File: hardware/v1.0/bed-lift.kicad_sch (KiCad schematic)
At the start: 64 parts, among them J1 SM04B-SRSS-TB, J2 S2P-VH, J3 SM04B-SRSS-TB, J4 S3B-XH-A, J5 S6B-XH-A, J6 Conn_ST_STDC14, J7 S6B-XH-A, J8 Conn_02x08_Odd_Even, Q1 MMBT3904, U1 LP2985-33DBVR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

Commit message: Review BOM.
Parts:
- C1, C11, C12, C13, C14, C15, C16, C2, C5, C8: Rating 50V, X5R -> 50V, X7R
- J8: now not fitted; now left out of the parts list
- U2: LCSC (none) -> C74511
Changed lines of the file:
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@@
 	(wire
 		(pts
-			(xy 118.11 214.63) (xy 124.46 214.63)
+			(xy 118.11 214.63) (xy 123.19 214.63)
 		)
 		(stroke
@@
 	(wire
 		(pts
-			(xy 120.65 203.2) (xy 124.46 203.2)
+			(xy 120.65 203.2) (xy 123.19 203.2)
 		)
 		(stroke
@@
 	(wire
 		(pts
-			(xy 119.38 200.66) (xy 124.46 200.66)
+			(xy 119.38 200.66) (xy 123.19 200.66)
 		)
 		(stroke
@@
 	(wire
 		(pts
-			(xy 118.11 209.55) (xy 124.46 209.55)
+			(xy 118.11 209.55) (xy 123.19 209.55)
 		)
 		(stroke
@@
 	(wire
 		(pts
-			(xy 121.92 205.74) (xy 124.46 205.74)
+			(xy 121.92 205.74) (xy 123.19 205.74)
 		)
 		(stroke
@@
 	(wire
 		(pts
-			(xy 118.11 217.17) (xy 124.46 217.17)
+			(xy 118.11 217.17) (xy 123.19 217.17)
 		)
 		(stroke
@@
 	(wire
 		(pts
-			(xy 118.11 219.71) (xy 124.46 219.71)
+			(xy 118.11 219.71) (xy 123.19 219.71)
 		)
 		(stroke
@@
 	(wire
 		(pts
-			(xy 118.11 212.09) (xy 124.46 212.09)
+			(xy 118.11 212.09) (xy 123.19 212.09)
 		)
 		(stroke
@@
 	)
 	(label "EXP_PA8"
-		(at 124.46 214.63 0)
+		(at 123.19 214.63 0)
 		(effects
 			(font
@@
 	)
 	(label "EXP_PB12"
-		(at 124.46 212.09 0)
+		(at 123.19 212.09 0)
 		(effects
 			(font
@@
 	)
 	(label "EXP_PA12"
-		(at 124.46 217.17 0)
+		(at 123.19 217.17 0)
 		(effects
 			(font
@@
 	)
 	(label "INT_I2C_SCL"
-		(at 124.46 209.55 0)
+		(at 123.19 209.55 0)
 		(effects
 			(font
@@
 	)
 	(label "SWCLK{slash}BOOT0"
-		(at 124.46 219.71 0)
+		(at 123.19 219.71 0)
 		(effects
 			(font
@@
 			)
 		)
-		(property "Rating" "50V, X5R"
+		(property "Rating" "50V, X7R"
 			(at 174.371 208.1064 0)
 			(effects
@@
 			)
 		)
-		(property "Rating" "50V, X5R"
+		(property "Rating" "50V, X7R"
 			(at 215.011 49.3564 0)
 			(effects
@@
 			)
 		)
-		(property "Rating" "50V, X5R"
+		(property "Rating" "50V, X7R"
 			(at 174.371 143.3364 0)
 			(effects
@@
 			)
 		)
-		(property "Rating" "50V, X5R"
+		(property "Rating" "50V, X7R"
 			(at 189.611 208.1064 0)
 			(effects
@@
 	(symbol
 		(lib_id "power:+5V")
-		(at 124.46 203.2 270)
+		(at 123.19 203.2 270)
 		(unit 1)
 		(exclude_from_sim no)
@@
 		(fields_autoplaced yes)
 		(property "Reference" "#PWR033"
-			(at 120.65 203.2 0)
+			(at 119.38 203.2 0)
 			(effects
 				(font
@@
 		)
 		(property "Value" "+5V"
-			(at 127.635 203.2 90)
+			(at 126.365 203.2 90)
 			(effects
 				(font
@@
 		)
 		(property "Footprint" ""
-			(at 124.46 203.2 0)
+			(at 123.19 203.2 0)
 			(effects
 				(font
@@
 		)
 		(property "Datasheet" ""
-			(at 124.46 203.2 0)
+			(at 123.19 203.2 0)
 			(effects
 				(font
@@
 		)
 		(property "Description" "Power symbol creates a global label with name \"+5V\""
-			(at 124.46 203.2 0)
+			(at 123.19 203.2 0)
 			(effects
 				(font
@@
 			)
 		)
-		(property "Rating" "50V, X5R"
+		(property "Rating" "50V, X7R"
 			(at 345.821 46.8164 0)
 			(effects
@@
 	(symbol
 		(lib_id "power:+3.3V")
-		(at 124.46 205.74 270)
+		(at 123.19 205.74 270)
 		(unit 1)
 		(exclude_from_sim no)
@@
 		(fields_autoplaced yes)
 		(property "Reference" "#PWR035"
-			(at 120.65 205.74 0)
+			(at 119.38 205.74 0)
 			(effects
 				(font
@@
 		)
 		(property "Value" "+3.3V"
-			(at 127.635 205.74 90)
+			(at 126.365 205.74 90)
 			(effects
 				(font
@@
 		)
 		(property "Footprint" ""
-			(at 124.46 205.74 0)
+			(at 123.19 205.74 0)
 			(effects
 				(font
@@
 		)
 		(property "Datasheet" ""
-			(at 124.46 205.74 0)
+			(at 123.19 205.74 0)
 			(effects
 				(font
@@
 		)
 		(property "Description" "Power symbol creates a global label with name \"+3.3V\""
-			(at 124.46 205.74 0)
+			(at 123.19 205.74 0)
 			(effects
 				(font
@@
 			)
 		)
-		(property "Rating" "50V, X5R"
+		(property "Rating" "50V, X7R"
 			(at 136.779 131.9064 0)
 			(effects
@@
 			)
 		)
+		(property "LCSC" "C74511"
+			(at 198.12 39.37 0)
+			(effects
+				(font
+					(size 1.27 1.27)
+				)
+				(hide yes)
+			)
+		)
 		(pin "1"
 		)
@@
 			)
 		)
-		(property "Rating" "50V, X5R"
+		(property "Rating" "50V, X7R"
 			(at 189.611 143.3364 0)
 			(effects
@@
 			)
 		)
-		(property "Rating" "50V, X5R"
+		(property "Rating" "50V, X7R"
 			(at 110.109 131.9064 0)
 			(effects
@@
 	(symbol
 		(lib_id "power:+12V")
-		(at 124.46 200.66 270)
+		(at 123.19 200.66 270)
 		(mirror x)
 		(unit 1)
@@
 		(fields_autoplaced yes)
 		(property "Reference" "#PWR030"
-			(at 120.65 200.66 0)
+			(at 119.38 200.66 0)
 			(effects
 				(font
@@
 		)
 		(property "Value" "+12V"
-			(at 127.635 200.66 90)
+			(at 126.365 200.66 90)
 			(effects
 				(font
@@
 		)
 		(property "Footprint" ""
-			(at 124.46 200.66 0)
+			(at 123.19 200.66 0)
 			(effects
 				(font
@@
 		)
 		(property "Datasheet" ""
-			(at 124.46 200.66 0)
+			(at 123.19 200.66 0)
 			(effects
 				(font
@@
 		)
 		(property "Description" "Power symbol creates a global label with name \"+12V\""
-			(at 124.46 200.66 0)
+			(at 123.19 200.66 0)
 			(effects
 				(font
@@
 		(unit 1)
 		(exclude_from_sim no)
-		(in_bom yes)
+		(in_bom no)
 		(on_board yes)
-		(dnp no)
+		(dnp yes)
 		(fields_autoplaced yes)
 		(property "Reference" "J8"
@@
 			)
 		)
-		(property "Rating" "50V, X5R"
+		(property "Rating" "50V, X7R"
 			(at 121.031 49.3564 0)
 			(effects
@@
 			)
 		)
-		(property "Rating" "50V, X5R"
+		(property "Rating" "50V, X7R"
 			(at 309.499 46.8164 0)
 			(effects

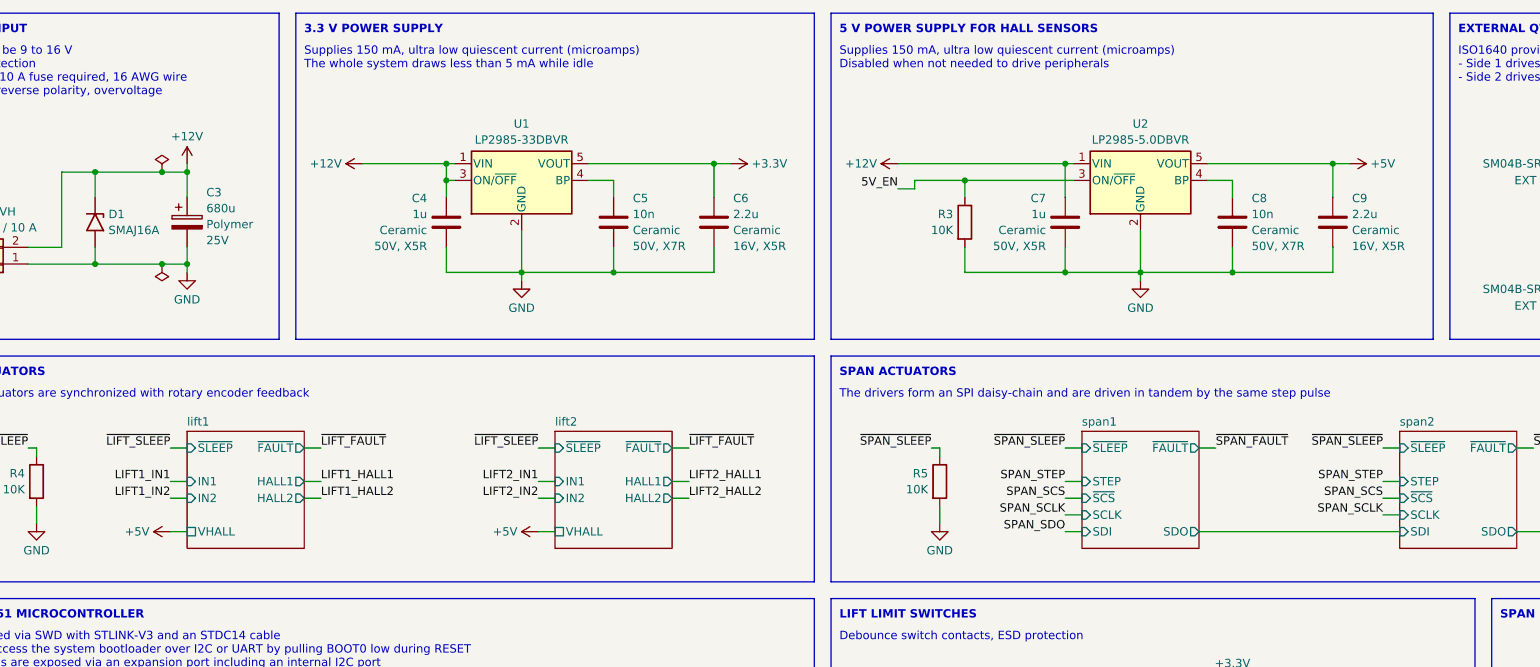
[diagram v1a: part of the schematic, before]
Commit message: Improve power distribution.
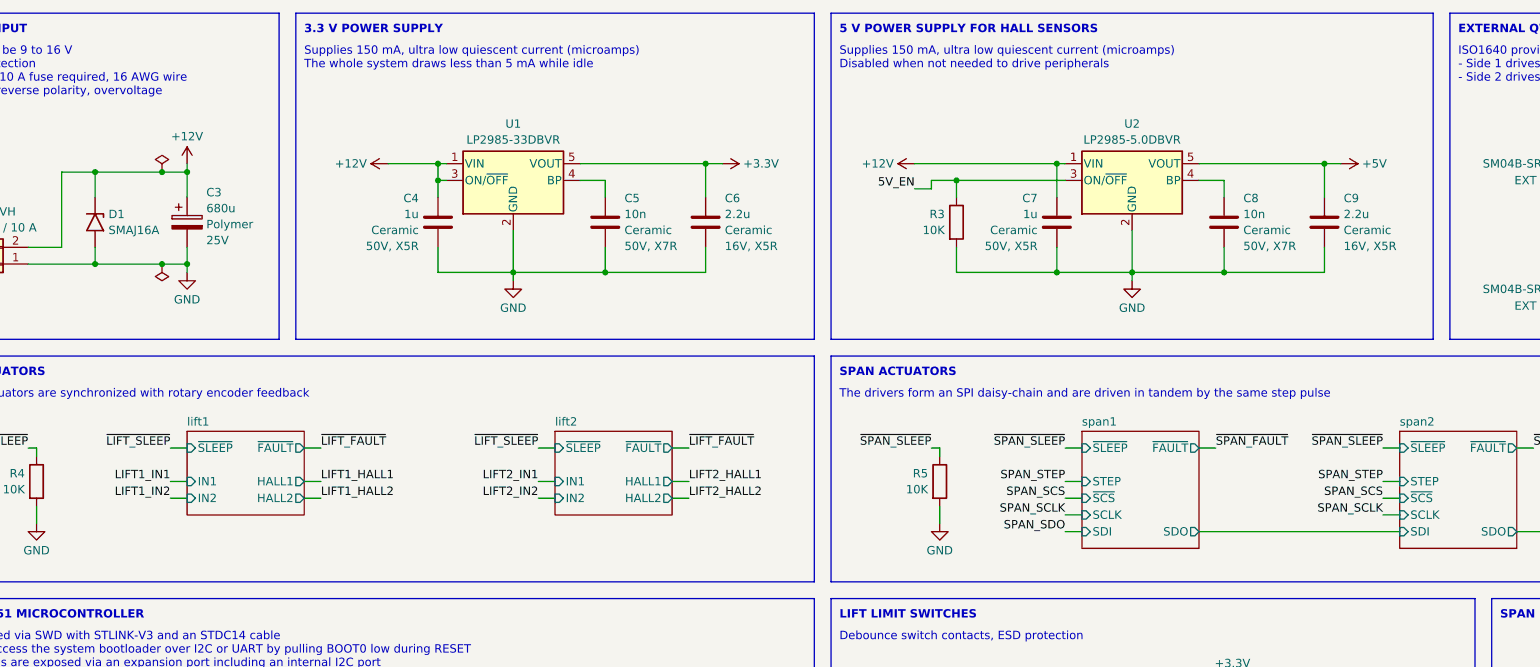
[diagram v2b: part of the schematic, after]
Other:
- sheet lift1 ports: added none; removed VHALL
- sheet lift2 ports: added none; removed VHALL
- moved on the sheet: C4, C5, C6, C7, C8, C9, R3, U1, U2

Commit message: Further refinement.
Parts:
- added C10: 1u, Capacitor_SMD:C_0603_1608Metric, symbol Device:C
- added D4: KT-0603R, LED_SMD:LED_0603_1608Metric, symbol Device:LED
- added D5: PESD3V3L5UY, Package_TO_SOT_SMD:SOT-363_SC-70-6, symbol Power_Protection:PESD3V3L5UY
- added J8: BM04B-SRSS-TB, Connector_JST:JST_SH_BM04B-SRSS-TB_1x04-1MP_P1.00mm_Vertical, symbol Connector_Generic_MountingPin:Conn_01x04_MountingPin
- added R29: 1K, Resistor_SMD:R_0402_1005Metric, symbol Device:R
- C1, C13, C14, C2: footprint Capacitor_SMD:C_0603_1608Metric -> Capacitor_SMD:C_0402_1005Metric; LCSC C14663 -> C1525; Rating 50V, X7R -> 16V, X7R
- C15: renamed from C12; footprint Capacitor_SMD:C_0603_1608Metric -> Capacitor_SMD:C_0402_1005Metric; LCSC C14663 -> C1525; Rating 50V, X7R -> 16V, X7R
- C16: renamed from C15; footprint Capacitor_SMD:C_0603_1608Metric -> Capacitor_SMD:C_0402_1005Metric; LCSC C14663 -> C1525; Rating 50V, X7R -> 16V, X7R
- C17: renamed from C16; footprint Capacitor_SMD:C_0603_1608Metric -> Capacitor_SMD:C_0402_1005Metric; LCSC C14663 -> C1525; Rating 50V, X7R -> 16V, X7R
- C5, C8: footprint Capacitor_SMD:C_0603_1608Metric -> Capacitor_SMD:C_0402_1005Metric; LCSC C57112 -> C15195
- J1, J3: Label EXT QWIIC -> EXT I2C
- R1, R12, R13, R14, R15, R16, R17, R2, R26, R28: footprint Resistor_SMD:R_0603_1608Metric -> Resistor_SMD:R_0402_1005Metric; LCSC C4190 -> C25879
- R10, R11, R20, R21, R6, R7, R8, R9: footprint Resistor_SMD:R_0603_1608Metric -> Resistor_SMD:R_0402_1005Metric; LCSC C31850 -> C25768
- R18: renamed from R29; footprint Resistor_SMD:R_0603_1608Metric -> Resistor_SMD:R_0402_1005Metric; LCSC C4190 -> C25879
- R19: renamed from R30; footprint Resistor_SMD:R_0603_1608Metric -> Resistor_SMD:R_0402_1005Metric; LCSC C4190 -> C25879
- R22: value 1K -> 3.3K; LCSC C21190 -> C4211
- R23, R24, R25: footprint Resistor_SMD:R_0603_1608Metric -> Resistor_SMD:R_0402_1005Metric; LCSC C22962 -> C25091
- R27, R3, R4, R5: footprint Resistor_SMD:R_0603_1608Metric -> Resistor_SMD:R_0402_1005Metric; LCSC C25804 -> C25744
- R30: renamed from R18; footprint Resistor_SMD:R_0603_1608Metric -> Resistor_SMD:R_0402_1005Metric; LCSC C25803 -> C25741
- R31: renamed from R19; footprint Resistor_SMD:R_0603_1608Metric -> Resistor_SMD:R_0402_1005Metric; LCSC C25803 -> C25741
- U2: value LP2985-5.0DBVR -> LP2985-50DBVR
- renumbered C10 to C11, C11 to C12, J8 to J6, J6 to J9
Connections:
- net +3.3V: now also D4.2 (A), J8.2 (Pin_2)
- net +5V: now also C10.1
- net BUS_GND: now also J1.MP (MountPin), J3.MP (MountPin)
- net CONSOLE_RX: now also D5.3 (K2)
- net CONSOLE_TX: now also D5.1 (K1)
- net EXP_PA12: now also J6.12 (Pin_12); no longer J6.14 (Pin_14)
- net GND: now also C10.2, D5.2 (A), J8.1 (Pin_1), J8.MP (MountPin)
- net INT_I2C_SCL: now also J8.4 (Pin_4)
- net INT_I2C_SDA: now also J8.3 (Pin_3)
- net SWCLK/BOOT0: now also D5.5 (K4)
- net SWDIO: now also D5.6 (K5)
- net ~{RESET}: now also D5.4 (K3)
- net EXP_PA8 renamed ~{LED_POWER}
- net ~{LED_POWER}: now also R29.2; no longer J6.12 (Pin_12)
- net LED_B renamed LED_STATUS_B
- net LED_G renamed LED_STATUS_G
- net LED_R renamed LED_STATUS_R
- new net: D4.1 (K), R29.1
- no-connect marks 6 -> 5
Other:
- note added: "EXTERNAL I2C INTERFACE (QWIIC)"
- note added: "Programmed via SWD with STLINK-V3 and an STDC14 cable Can also access the system bootloader over I2C or UART by pulling BOOT0 low during RESET Unused pins are exposed via an expansion port including an internal I2C interface (QWIIC)"
- note removed: "EXTERNAL QWIIC INTERFACE"
- note removed: "Programmed via SWD with STLINK-V3 and an STDC14 cable Can also access the system bootloader over I2C or UART by pulling BOOT0 low during RESET Unused pins are exposed via an expansion port including an internal I2C port"
- moved on the sheet: C11, C12, C15, J5, J6, J9, R18, R19, R30, R31
